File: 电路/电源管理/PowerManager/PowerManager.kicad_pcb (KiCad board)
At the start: 2 copper layers, 41.5 x 25 mm, 30 parts, among them Q1 IRF7324TRPBF, U1 TPS61288LRQQR, U2 ZX-ZH1.5-2PWT, U3 ZX-PH2.0-WT4P, U8 ZX-XH2.54-5PWT

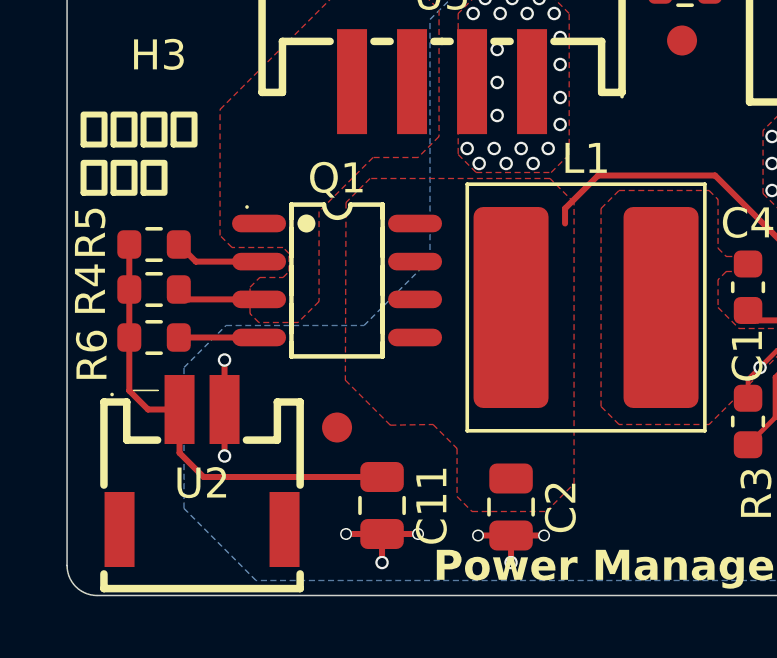
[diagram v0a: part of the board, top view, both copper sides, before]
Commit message: 保存主控电源PCB与Rev3结构及导出模型更新
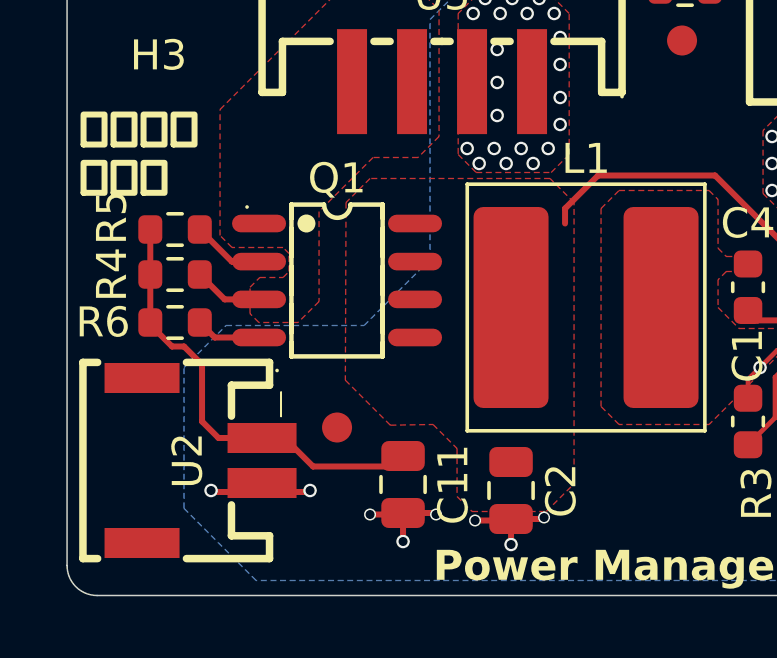
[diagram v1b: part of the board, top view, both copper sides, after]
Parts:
- moved C11 0.99 mm to (101.5, 82.5)
- moved R4 0.86 mm to (93.9, 75.5)
- moved R5 0.86 mm to (93.9, 74.0)
- moved R6 0.86 mm to (93.9, 77.1)
- moved C2 0.55 mm to (105.1, 82.7)
- moved U2 0.30 mm to (94.8, 81.7), turned to -90 degrees
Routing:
- net /SWITCH: track 15.3 -> 14.8 mm
